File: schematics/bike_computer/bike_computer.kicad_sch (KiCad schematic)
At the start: 0 parts

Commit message: schematic updates for bike computer, rear light unit, rear light unit control box
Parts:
- added U1: ESP32-WROOM-32, RF_Module:ESP32-WROOM-32, symbol RF_Module:ESP32-WROOM-32
- added U2: SHT31-DIS, Sensor_Humidity:Sensirion_DFN-8-1EP_2.5x2.5mm_P0.5mm_EP1.1x1.7mm, symbol Sensor_Humidity:SHT31-DIS
- added U3: BMP280, Package_LGA:Bosch_LGA-8_2x2.5mm_P0.65mm_ClockwisePinNumbering, symbol Sensor_Pressure:BMP280
- added U4: TFT LCD ST7796, ..., symbol FarrhadTech:TFT_LCD_display
- added U6: RYS352A, symbol FarrhadTech:RYS352A
- added U7: TP4056 module, ..., symbol FarrhadTech:TP4056
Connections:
- new net: U1.19 (SCS/CMD), U1.20 (SCK/CLK), U3.2 (CSB), U3.4 (SCK), U4.10 (T_CLK), U4.11 (T_CS), U4.3 (CS), U4.7 (SCK)
- new net: U1.21 (SDO/SD0), U3.3 (SDI), U4.12 (T_DIN), U4.6 (SDI(MOSI))
- new net: U1.22 (SDI/SD1), U3.5 (SDO), U4.13 (T_DO), U4.9 (SDO(MISO))
- new net: U1.35 (TXD0/IO1), U6.3 (TXD)
- new net: U1.34 (RXD0/IO3), U6.4 (RXD)
- new net: U1.24 (IO2), U6.6 (RESET_N)
- new net: U1.7 (IO35), U4.14 (T_IRQ)
- new net: U1.13 (IO14), U4.4 (RESET)
- new net: U1.23 (IO15), U4.5 (DC/RS)
- new net: U1.27 (IO16), U4.8 (LED)
- new net: U1.12 (IO27), U2.6 (~{RESET})
- new net: U1.6 (IO34), U2.3 (ALERT)
- new net: U1.8 (IO32), U2.1 (SDA)
- new net: U1.9 (IO33), U2.4 (SCL)
- new net +3.3V: U1.2 (VDD), U2.5 (VDD), U3.6 (VDDIO), U3.8 (VDD), U4.1 (VCC), U6.5 (VCC)
- new net GND: U1.1 (GND), U1.15 (GND), U1.38 (GND), U1.39 (GND), U2.2 (ADDR), U2.7 (R), U2.8 (VSS), U2.9 (VSS), U3.1 (GND), U3.7 (GND), U4.2 (GND), U6.10 (GND), U6.11 (GND), U6.12 (GND), U6.2 (GND), U6.7 (GND), U6.8 (GND), U6.9 (GND), U7.2 (GND_USB)
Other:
- note added: "480x320 TFT LCD display"
- note added: "GNSS module"
- note added: "USB charging and battery protection"
- note added: "atmospheric pressure/ altitude sensor"
- note added: "temperature/ humidity sensor"

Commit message: more schematic updates
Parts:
- removed U7: TP4056 module, ..., symbol FarrhadTech:TP4056
- added BT1: Battery_Cell, symbol Device:Battery_Cell
- added SW1: rocker_switch, symbol Switch:SW_SPST
- added U5: TP4056 module, ..., symbol FarrhadTech:TP4056
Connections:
- net +3.3V: now also SW1.2 (B)
- net GND: now also U5.5 (OUT-)
- net at U1.19 (SCS/CMD), U3.2 (CSB), U4.11 (T_CS)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: no longer U1.20 (SCK/CLK), U3.4 (SCK), U4.10 (T_CLK), U4.7 (SCK)
- new net: SW1.1 (A), U5.5 (OUT-)
- new net: U1.20 (SCK/CLK), U3.4 (SCK), U4.10 (T_CLK), U4.7 (SCK)
- new net: BT1.1 (+), U5.3 (B+)
- new net: BT1.2 (-), U5.4 (B-)
- no-connect marks 0 -> 2
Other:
- note added: "DEVKITV1"
- note added: "GNSS module breakout board"
- note added: "NOTES I have not added bypass caps/any other external components for the sensors because they are contained on small development boards which already implement these components. Since the boards are rather small, I will simply solder those on to the PCBs as-is."
- note added: "Samsung 30Q 18650 (3000 mAH, 3.7 V nominal)"
- note added: "This switch connects the rest of the system to the battery for power. Make sure it is turned to the "off" position when charging the battery to ensure correct operation!"
- note added: "atmospheric pressure, altitude sensor breakout board"
- note added: "temperature, humidity sensor breakout board"
- note removed: "GNSS module"
- note removed: "USB charging and battery protection"
- note removed: "atmospheric pressure/ altitude sensor"
- note removed: "temperature/ humidity sensor"

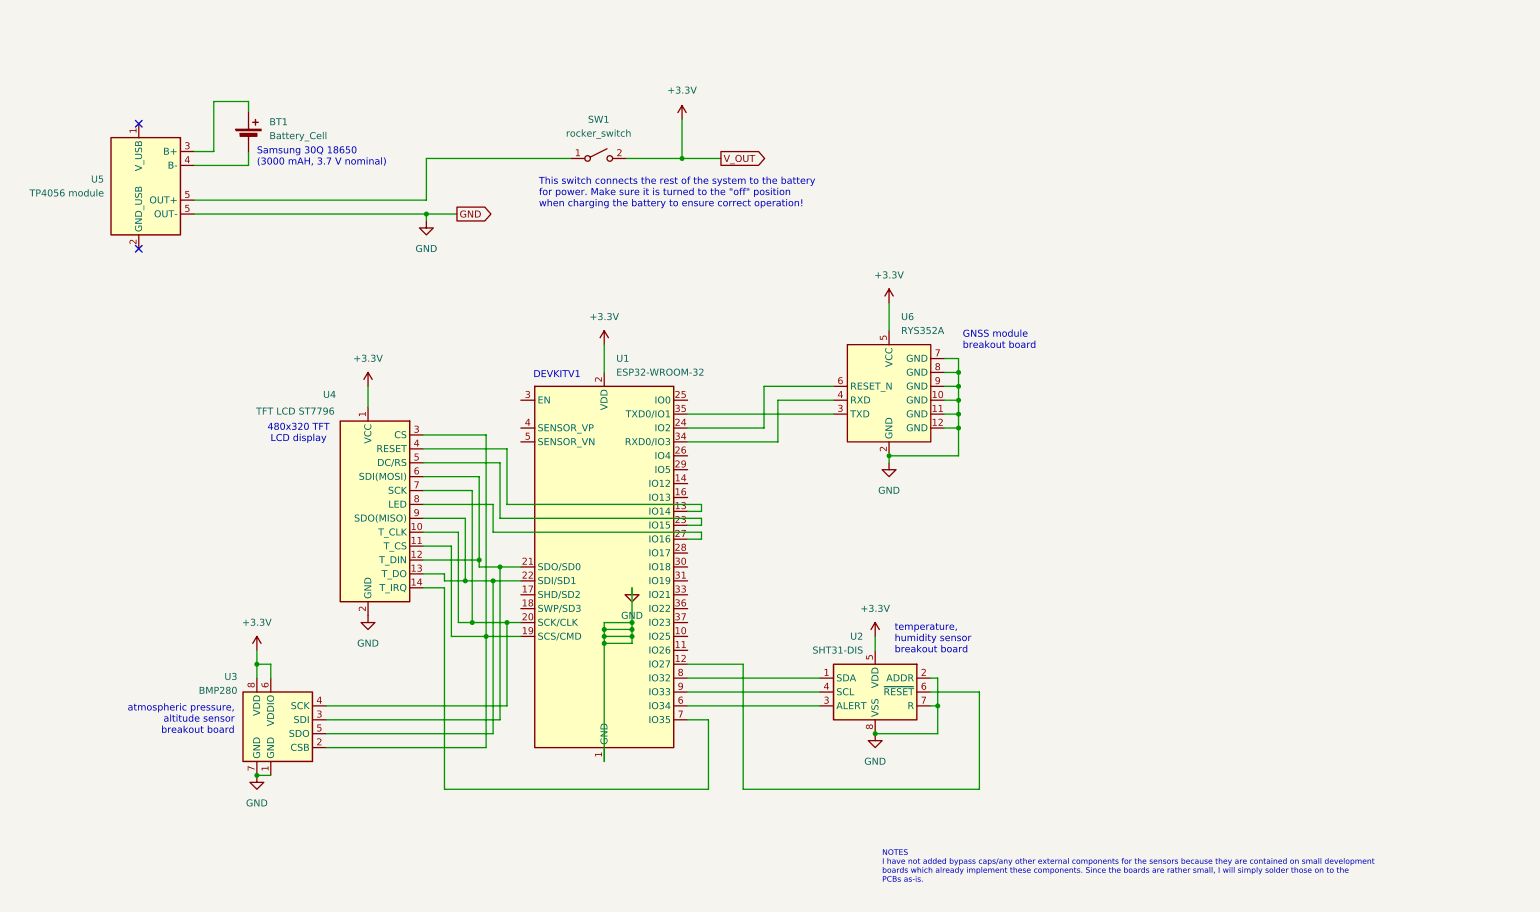
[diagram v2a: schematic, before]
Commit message: more schematic updates: re-did bike computer with better ESP32 symbol, fixed component data on other schematics (somehow some of the part nums, descriptions, etc disappeared??)
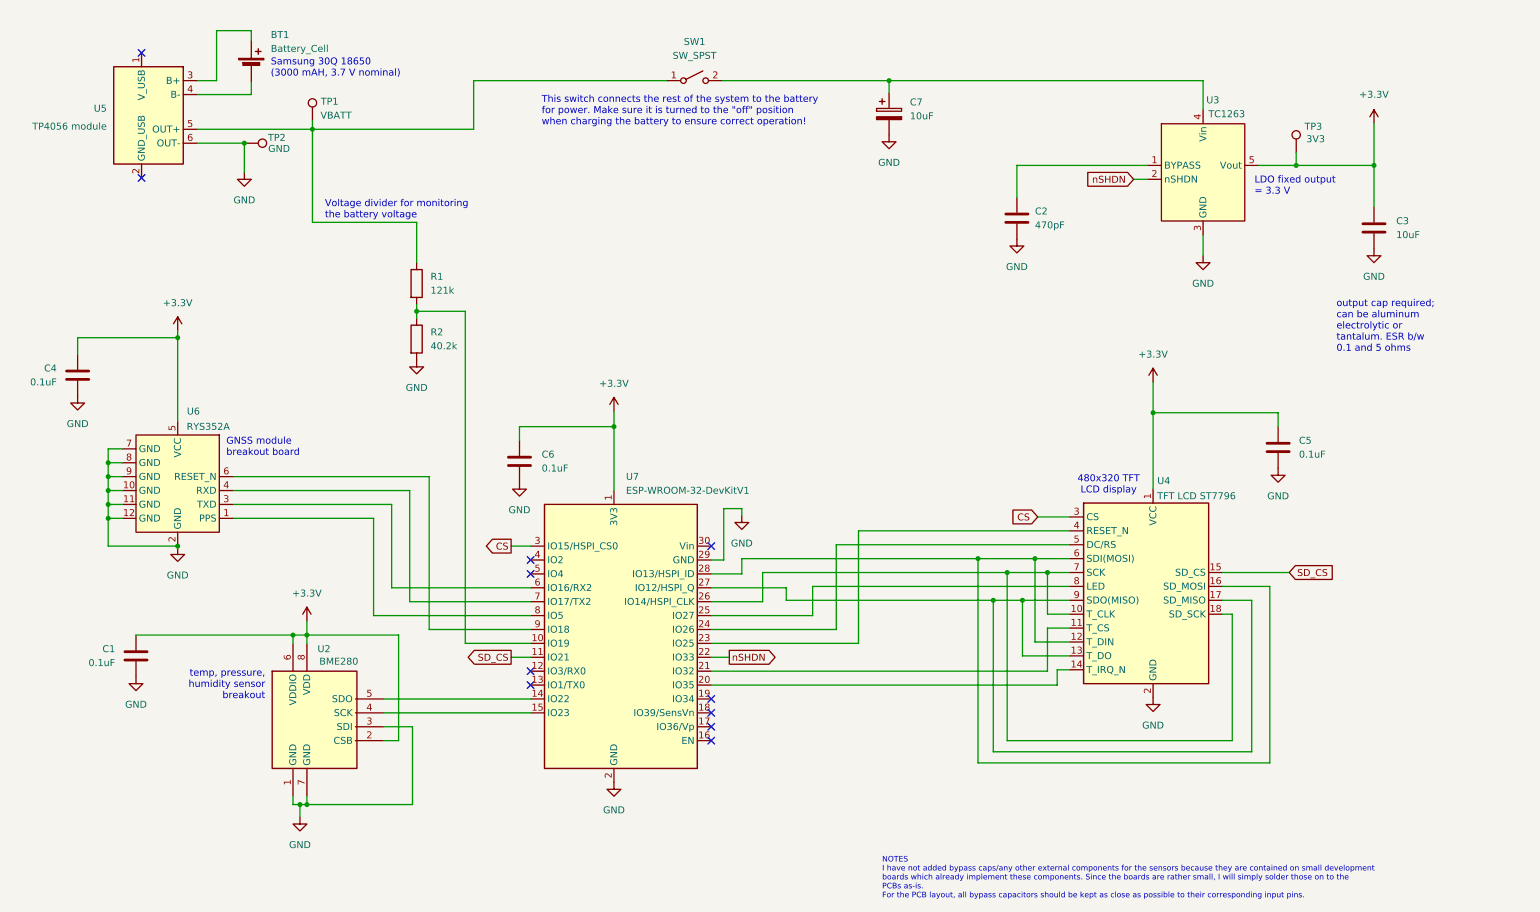
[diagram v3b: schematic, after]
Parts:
- removed U1: ESP32-WROOM-32, RF_Module:ESP32-WROOM-32, symbol RF_Module:ESP32-WROOM-32
- removed U2: SHT31-DIS, Sensor_Humidity:Sensirion_DFN-8-1EP_2.5x2.5mm_P0.5mm_EP1.1x1.7mm, symbol Sensor_Humidity:SHT31-DIS
- removed U3: BMP280, Package_LGA:Bosch_LGA-8_2x2.5mm_P0.65mm_ClockwisePinNumbering, symbol Sensor_Pressure:BMP280
- added C1, C4, C5, C6: 0.1uF, Capacitor_THT:C_Rect_L4.6mm_W2.0mm_P2.50mm_MKS02_FKP02, symbol Device:C
- added C2: 470pF, Capacitor_THT:C_Rect_L4.6mm_W2.0mm_P2.50mm_MKS02_FKP02, symbol Device:C
- added C3: 10uF, Capacitor_THT:CP_Radial_D5.0mm_P2.00mm, symbol Device:C
- added C7: 10uF, Capacitor_THT:CP_Radial_D5.0mm_P2.00mm, symbol Device:C_Polarized
- added R1: 121k, Resistor_THT:R_Axial_DIN0207_L6.3mm_D2.5mm_P10.16mm_Horizontal, symbol Device:R
- added R2: 40.2k, Resistor_THT:R_Axial_DIN0207_L6.3mm_D2.5mm_P10.16mm_Horizontal, symbol Device:R
- added TP1: VBATT, TestPoint:TestPoint_Keystone_5000-5004_Miniature, symbol Connector:TestPoint
- added TP2: GND, TestPoint:TestPoint_Keystone_5000-5004_Miniature, symbol Connector:TestPoint
- added TP3: 3V3, TestPoint:TestPoint_Keystone_5000-5004_Miniature, symbol Connector:TestPoint
- added U2: BME280, FarrhadTech:BME280_module, symbol FarrhadTech:BME280
- added U3: TC1263, FarrhadTech:TO-220-3_Horizontal_TabUpNoHole, symbol FarrhadTech:TC1263
- added U7: ESP-WROOM-32-DevKitV1, FarrhadTech:ESP-WROOM-32_DevKitV1, symbol FarrhadTech:ESP-WROOM-32-DevKitV1
- BT1: footprint (none) -> FarrhadTech:BatteryHolder_18650; Part Num (none) -> Samsung 30Q 18650
- SW1: value rocker_switch -> SW_SPST; footprint (none) -> Button_Switch_THT:SW_Lever_1P2T_NKK_GW12LxH; Part Num (none) -> GW12LCH
- U4: footprint ... -> FarrhadTech:Display_420x380; Part Num (none) -> Hosyond TFT LCD 480x320
- U5: footprint ... -> FarrhadTech:TP4056_module; Part Num (none) -> TP4056 module
- U6: footprint (none) -> FarrhadTech:RYS352A; Part Num (none) -> REYAX RYS352A
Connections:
- net +3.3V: now also C1.1, C3.1, C4.1, C5.1, C6.1, TP3.1, U2.2 (CSB), U2.6 (VDDIO), U2.8 (VDD), U3.5 (Vout), U7.1 (3V3); no longer SW1.2 (B)
- net GND: now also U5.6 (OUT-), C1.2, C2.2, C3.2, C4.2, C5.2, C6.2, C7.2, R2.2, TP2.1, U2.1 (GND), U2.3 (SDI), U2.7 (GND), U3.3 (GND), U7.2 (GND), U7.29 (GND); no longer U5.5 (OUT-)
- net at SW1.1 (A), U5.5 (OUT+): now also R1.1, TP1.1
- net at U4.11 (T_CS): now also U7.21 (IO32); no longer U4.3 (CS)
- net at U4.12 (T_DIN), U4.6 (SDI(MOSI)): now also U4.16 (SD_MOSI), U7.28 (IO13/HSPI_ID)
- net at U4.10 (T_CLK), U4.7 (SCK): now also U4.18 (SD_SCK), U7.26 (IO14/HSPI_CLK)
- net at U4.13 (T_DO), U4.9 (SDO(MISO)): now also U4.17 (SD_MISO), U7.27 (IO12/HSPI_Q)
- net at U6.3 (TXD): now also U7.6 (IO16/RX2)
- net at U6.4 (RXD): now also U7.7 (IO17/TX2)
- net at U6.6 (RESET_N): now also U7.9 (IO18)
- net at U4.14 (T_IRQ_N): now also U7.20 (IO35)
- net at U4.4 (RESET_N): now also U7.23 (IO25)
- net at U4.5 (DC/RS): now also U7.24 (IO26)
- net at U4.8 (LED): now also U7.25 (IO27)
- new net: C7.1, SW1.2 (B), U3.4 (Vin)
- new net: U6.1 (PPS), U7.8 (IO5)
- new net: R1.2, R2.1, U7.10 (IO19)
- new net: U2.5 (SDO), U7.14 (IO22)
- new net: U2.4 (SCK), U7.15 (IO23)
- new net: C2.1, U3.1 (BYPASS)
- new net CS: U4.3 (CS), U7.3 (IO15/HSPI_CS0)
- new net SD_CS: U4.15 (SD_CS), U7.11 (IO21)
- new net nSHDN: U3.2 (nSHDN), U7.22 (IO33)
- no-connect marks 2 -> 11
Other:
- note added: "LDO fixed output = 3.3 V"
- note added: "NOTES I have not added bypass caps/any other external components for the sensors because they are contained on small development boards which already implement these components. Since the boards are rather small, I will simply solder those on to the PCBs as-is. For the PCB layout, all bypass capacitors should be kept as close as possible to their corresponding input pins."
- note added: "Voltage divider for monitoring the battery voltage"
- note added: "output cap required; can be aluminum electrolytic or tantalum. ESR b/w 0.1 and 5 ohms"
- note added: "temp, pressure, humidity sensor breakout"
- note removed: "DEVKITV1"
- note removed: "NOTES I have not added bypass caps/any other external components for the sensors because they are contained on small development boards which already implement these components. Since the boards are rather small, I will simply solder those on to the PCBs as-is."
- note removed: "atmospheric pressure, altitude sensor breakout board"
- note removed: "temperature, humidity sensor breakout board"
- moved on the sheet: BT1, SW1, U5

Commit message: bike computer layout v0
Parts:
- removed SW1: SW_SPST, Button_Switch_THT:SW_Lever_1P2T_NKK_GW12LxH, symbol Switch:SW_SPST
- added SW1: GW12LxH, FahrradTech:SW_Lever_1P2T_NKK_GW12LxH, symbol FarrhadTech:GW12LxH
- BT1: footprint FarrhadTech:BatteryHolder_18650 -> FahrradTech:BatteryHolder_18650
- TP1, TP2, TP3: footprint TestPoint:TestPoint_Keystone_5000-5004_Miniature -> FahrradTech:TestPoint_Keystone_5000-5004_Miniature
- U2: footprint FarrhadTech:BME280_module -> FahrradTech:BME280_module
- U3: footprint FarrhadTech:TO-220-3_Horizontal_TabUpNoHole -> FahrradTech:TO-220-5_P3.4x3.8mm_StaggerOdd_Lead7.13mm_TabDown
- U4: footprint FarrhadTech:Display_420x380 -> FahrradTech:Display_420x380
- U5: footprint FarrhadTech:TP4056_module -> FahrradTech:TP4056_module
- U6: footprint FarrhadTech:RYS352A -> FahrradTech:RYS352A
- U7: footprint FarrhadTech:ESP-WROOM-32_DevKitV1 -> FahrradTech:ESP-WROOM-32_DevKitV1
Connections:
- net GND: now also U2.5 (SDO); no longer U2.3 (SDI)
- net at R1.1, TP1.1, U5.5 (OUT+): now also SW1.5
- net at C7.1, U3.4 (Vin): now also SW1.6
- net at U7.14 (IO22): now also U2.4 (SCK); no longer U2.5 (SDO)
- net at U7.15 (IO23): now also U2.3 (SDI); no longer U2.4 (SCK)
- no-connect marks 11 -> 12
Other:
- note removed: "NOTES I have not added bypass caps/any other external components for the sensors because they are contained on small development boards which already implement these components. Since the boards are rather small, I will simply solder those on to the PCBs as-is. For the PCB layout, all bypass capacitors should be kept as close as possible to their corresponding input pins."
- title: FarrhadTech Bike Computer -> FahrradTech Bike Computer
